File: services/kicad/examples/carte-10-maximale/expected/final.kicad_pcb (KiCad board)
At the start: 4 copper layers, 60.9 x 45.7 mm, 70 parts, among them J1 IN_5V, J10 IO0, J11 IO1, J12 IO2, J13 IO3, J14 IO4, J2 SWD, U1 STM32F103C8T6, U2 AMS1117-3.3

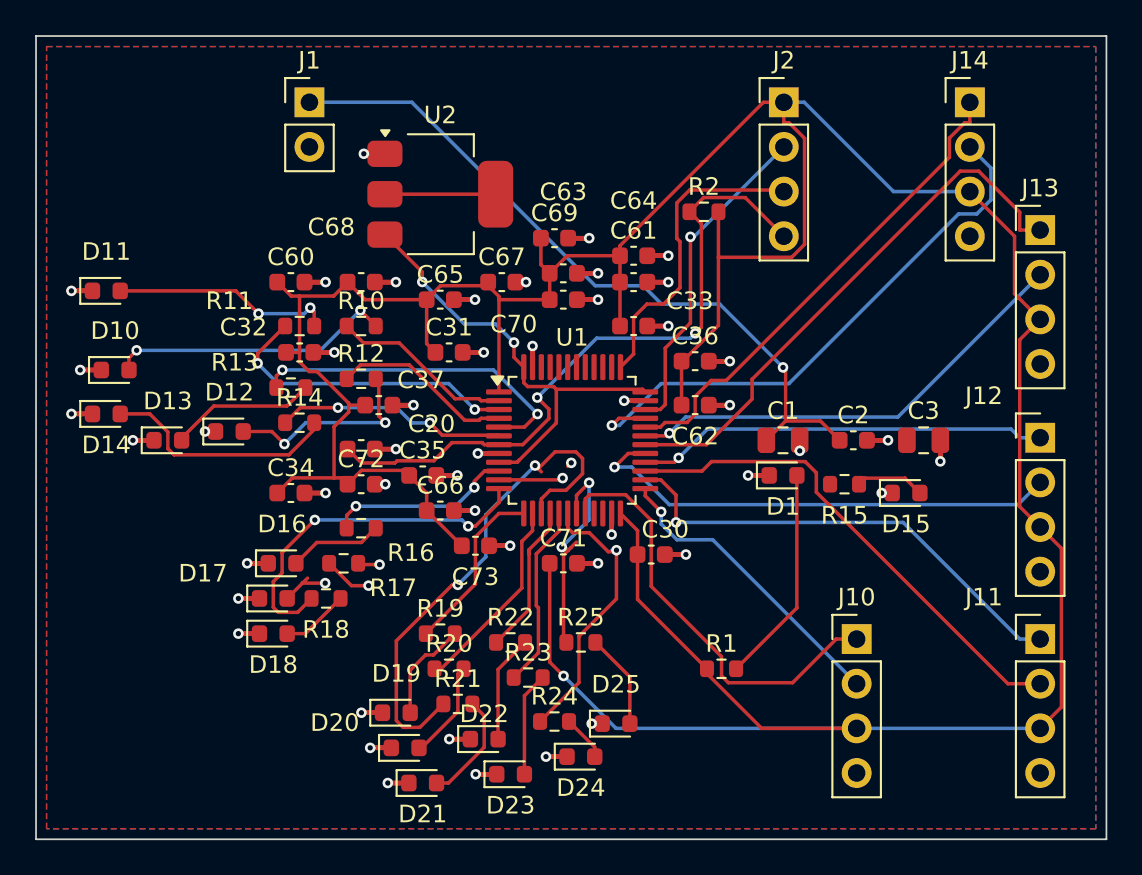
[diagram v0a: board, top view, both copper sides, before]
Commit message: feat(placement): les peripheriques se REPARTISSENT, ils ne s empilent plus
Question de l utilisateur devant le rendu : « c est quoi ce type de placement ? ».
Les composants s entassaient d un seul cote du boitier, etiquettes de
serigraphie l une sur l autre, trois quarts de la couronne vides.

TROIS CAUSES, toutes dans `_poser_les_peripheriques`, toutes la meme faute —
un angle unique pour tout un groupe :

  - les DIRECTS qui visent la meme broche (tous les decouplages d un rail,
    toutes les resistances d un meme signal) recevaient le MEME `angle_vers`
    et le meme rayon de depart ;
  - les SUIVEURS d un meme parent recevaient tous atan2(parent - centre) ;
  - les ISOLES partaient tous de l angle 0.0, c est-a-dire du meme point.

`le_long_du_rayon` ne s ecartait qu une fois la place prise : d ou la file.

REMEDE : `_ecart_en_eventail`. Le PREMIER de chaque groupe garde EXACTEMENT la
direction calculee — c est la topologie, on ne la perd pas pour faire joli — et
les suivants s ecartent symetriquement de 3 x `_PAS_ANGLE_DEG`.
Rien de deja pose ne bouge : seul l ANGLE DE DEPART de la recherche change, et
`le_long_du_rayon` reste seul juge de ce qui est libre.

BANC DES DIX CARTES, contour resserre ET peripheriques repartis :

    carte             demandee    livree         err  manq
    carte-01           25 x 20    20,1 x 13,6     0    0
    carte-02           55 x 40    34,9 x 25,2     0    0
    carte-03           50 x 35    27,6 x 19,9     0    0
    carte-04           60 x 45    36,6 x 29,8     0    0
    carte-05           70 x 50    40,0 x 32,6     0    0
    carte-06           80 x 60    46,5 x 36,4     0    0
    carte-07          110 x 80    47,7 x 38,8     0    0
    carte-08          125 x 95    57,4 x 44,1     0    0
    carte-09          130 x 100   57,8 x 45,2     0    0
    carte-10          140 x 105   59,0 x 45,8     0    0

Dix sur dix, 100 % route. carte-07 gagne 5,5 mm de largeur sur le passage
precedent, carte-06 deux, carte-10 deux. Sur ca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
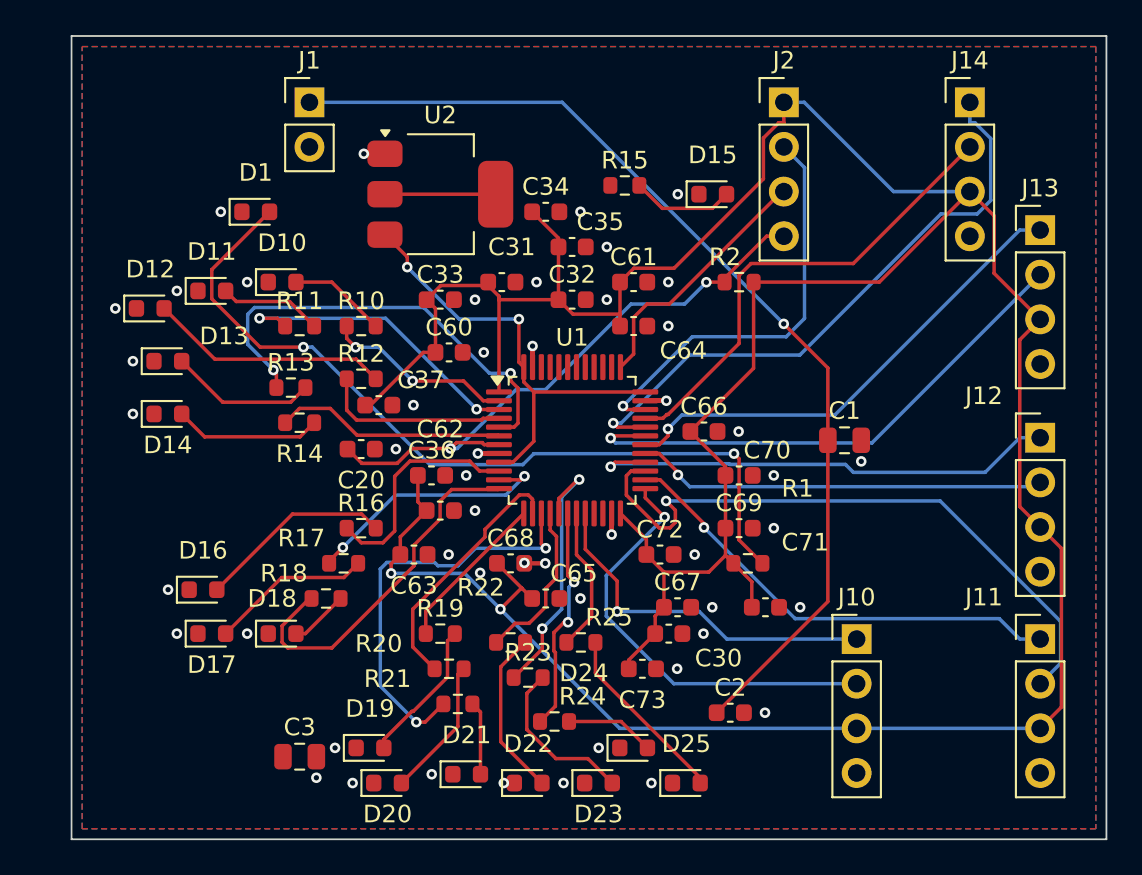
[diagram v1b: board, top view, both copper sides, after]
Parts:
- moved C3 39.8 mm to (93.5, 93.5)
- moved D1 33.5 mm to (91.0, 62.5)
- moved C34 21.6 mm to (107.5, 62.5)
- moved R15 21.1 mm to (112.0, 61.0)
- moved C67 21.0 mm to (115.0, 85.0)
- moved D15 20.2 mm to (117.0, 61.5)
- moved C69 19.6 mm to (118.5, 80.5)
- moved C63 18.1 mm to (100.0, 82.0)
- moved C68 18.1 mm to (105.5, 82.5)
- moved C65 18.0 mm to (107.5, 84.5)
- moved C72 17.5 mm to (114.0, 82.0)
- moved C2 17.0 mm to (118.0, 91.0)
- moved C36 16.3 mm to (101.0, 77.5)
- moved C32 15.8 mm to (109.0, 67.5)
- moved C62 15.7 mm to (101.5, 79.5)
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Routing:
- net GND: track 166.8 -> 15.6 mm, vias 48 -> 50
- net LED_PWR: track 12.4 -> 47.1 mm, vias 0 -> 2
- net VIN: track 41.4 -> 58.0 mm
- net LEDA0: track 16.2 -> 5.57 mm, vias 2 -> 0
- net IO_L14: track 22.4 -> 13.0 mm
- net +3V3: track 207.6 -> 198.8 mm, vias 1 -> 2
- net EXT1_2: track 28.6 -> 36.7 mm, vias 0 -> 1
- net EXT0_2: track 17.3 -> 24.9 mm
- net EXT4_1: track 28.0 -> 34.9 mm, vias 0 -> 1
- net LEDA1: track 12.6 -> 5.87 mm, vias 2 -> 0
- net IO_L3: track 19.2 -> 25.7 mm
- net IO_L11: track 29.6 -> 23.7 mm
- net LEDA6: track 5.37 -> 11.2 mm
- net EXT4_2: track 32.5 -> 27.1 mm, vias 1 -> 0
- net NRST: track 38.9 -> 33.6 mm
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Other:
- board size 60.9 x 45.7 mm -> 58.9 x 45.7 mm
- copper layers 4 -> 2

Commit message: docs(banc): les dix boards du banc du 2026-09-23, service corrige
Artefacts du banc dont le tableau est deja commite : les dix cartes a
100 % route, 0 erreur, 0 connexion manquante, chacune a la taille de son
circuit.

Co-Authored-By: Claude Opus 5 <noreply@anthropic.com>
Claude-Session: https://claude.ai/code/session_01TnMqm4La2CxQHHB5K8aSSV
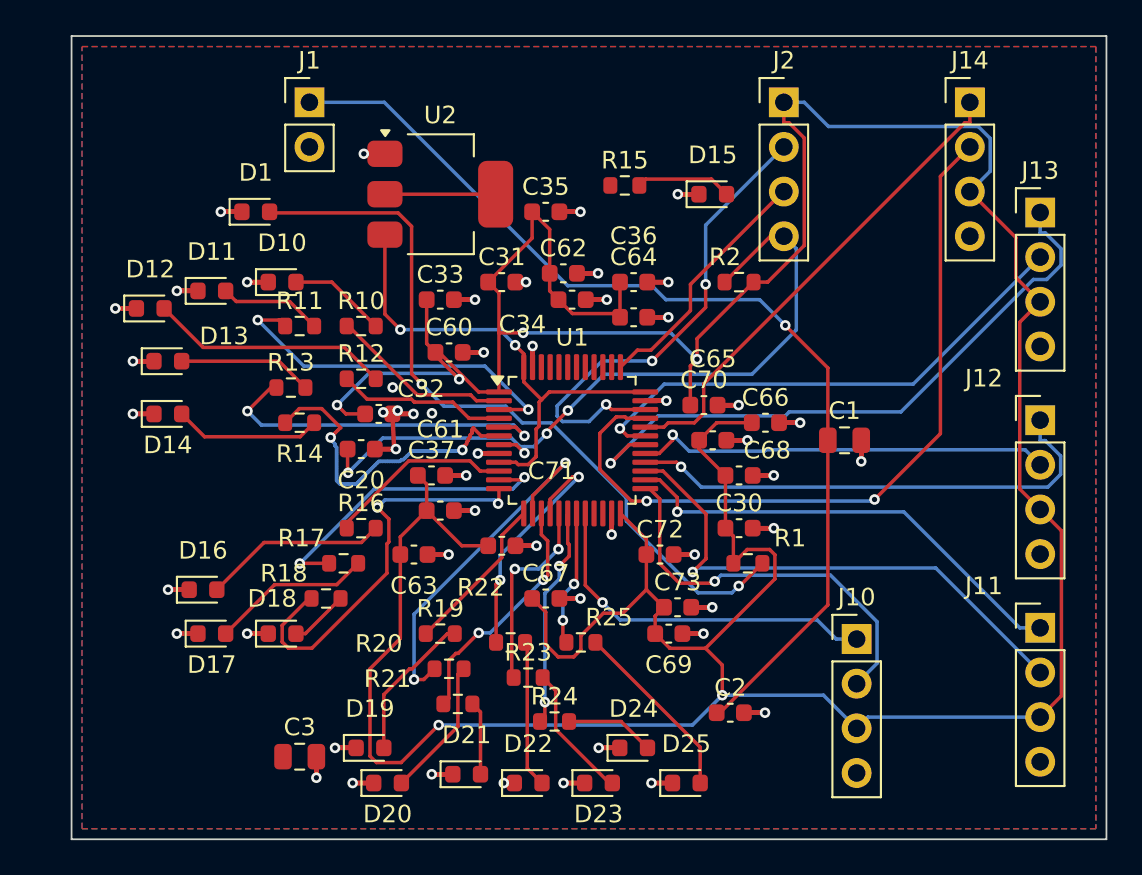
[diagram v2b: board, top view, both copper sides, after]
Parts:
- moved C61 17.0 mm to (101.5, 79.5)
- moved C71 15.4 mm to (105.0, 81.5)
- moved C62 15.2 mm to (108.5, 66.0)
- moved C36 14.6 mm to (112.5, 68.5)
- moved C68 13.9 mm to (118.5, 77.5)
- moved C65 13.1 mm to (117.0, 75.5)
- moved C32 12.8 mm to (98.0, 74.0)
- moved C67 7.52 mm to (107.5, 84.5)
- moved C30 7.21 mm to (118.5, 80.5)
- moved C69 7.21 mm to (114.5, 86.5)
- moved C34 5.22 mm to (109.0, 67.5)
- moved C37 5.00 mm to (101.0, 77.5)
- moved C70 4.47 mm to (116.5, 73.5)
- moved C73 4.03 mm to (115.0, 85.0)
- moved C66 3.54 mm to (120.0, 74.5)
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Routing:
- net GND: track 15.6 -> 175.9 mm, vias 50 -> 52
- net +3V3: track 198.8 -> 234.1 mm, vias 2 -> 6
- net EXT4_2: track 27.1 -> 43.8 mm, vias 0 -> 2
- net IO_L11: track 23.7 -> 13.9 mm
- net NRST: track 33.6 -> 42.8 mm, vias 2 -> 4
- net EXT3_1: track 27.8 -> 36.4 mm
- net EXT4_1: track 34.9 -> 27.8 mm, vias 1 -> 0
- net IO_L10: track 14.6 -> 21.0 mm, vias 0 -> 2
- net EXT1_2: track 36.7 -> 30.4 mm
- net IO_L3: track 25.7 -> 20.2 mm
- net IO_L4: track 13.1 -> 18.6 mm, vias 0 -> 2
- net IO_L12: track 9.38 -> 14.3 mm, vias 0 -> 2
- net SWDIO: track 24.0 -> 28.0 mm, vias 1 -> 3
- net IO_L13: track 15.3 -> 11.3 mm
- net LED_PWR: track 47.1 -> 43.4 mm
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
